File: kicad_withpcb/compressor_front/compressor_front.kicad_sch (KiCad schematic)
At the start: 33 parts, among them J1 MAIN BOARD, SW1 BYPASS, SW2 INT/EXT, SW3 HPF DEFEAT, SW4 LINK, U10 LM3915, U9 LM3914

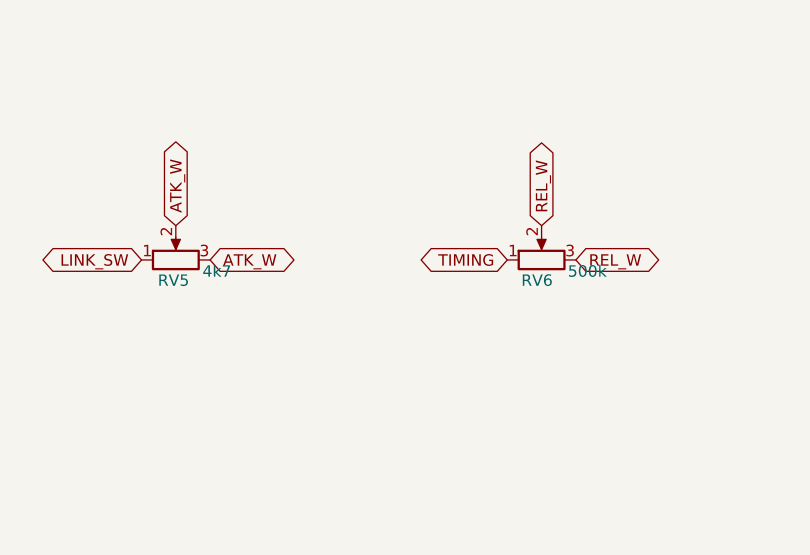
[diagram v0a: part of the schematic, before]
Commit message: Fit real film capacitors on the main board and use Altronics pots for RV5/RV6
RV5 (ATTACK) goes 4k7 -> 10k and RV6 (RELEASE) 500k -> 1M, the nearest
Altronics 9 mm values (R1946, R1950), on the split sheets, both boards
and design.py; the Sim.Params follow (R=10000, R=1e+06).

C5, C8, C9, C10, C14, C15 and C35 were drawn as 7 x 2.5 mm on 5 mm, which
no 2.2-10 uF film part fits. They now use stock KiCad footprints for
in-stock element14 parts:
  10 uF  C5 C8 C15  TDK B32562H1106K000   C_Rect_L16.5mm_W11.8mm_P15.00mm_MKT
  4.7 uF C9 C10     TDK B32562H1475K000   C_Rect_L16.5mm_W7.3mm_P15.00mm_MKT
  2.2 uF C14 C35    KEMET MMK5225K63J06L4 C_Rect_L7.2mm_W7.2mm_P5.00mm_FKS2...

To make room, small parts were re-placed by script (the caps near their
old spots, displaced parts re-homed, then same-footprint parts swapped to
cut wire length; transistors, ICs, connectors and trimmers did not move)
and the main board was re-routed with Freerouting, keeping the original
card-finger stubs. DRC 0 errors, 0 unconnected, schematic parity clean;
ERC 0 errors. The BOM names the element14 parts.
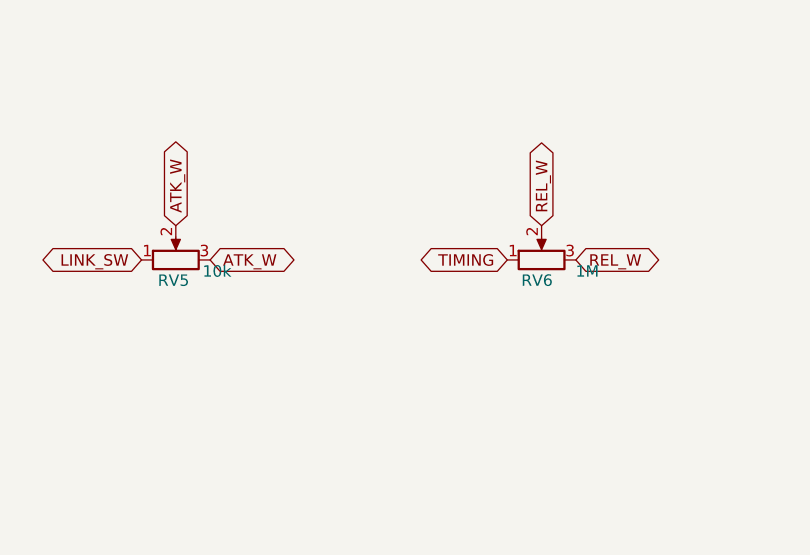
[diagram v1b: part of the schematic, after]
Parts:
- RV5: value 4k7 -> 10k
- RV6: value 500k -> 1M
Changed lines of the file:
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@@
 			)
 		)
-		(property "Value" "500k"
+		(property "Value" "1M"
 			(at 275.59 50.8 90)
 			(show_name no)
@@
 			)
 		)
-		(property "Value" "4k7"
+		(property "Value" "10k"
 			(at 234.442 50.8 90)
 			(show_name no)

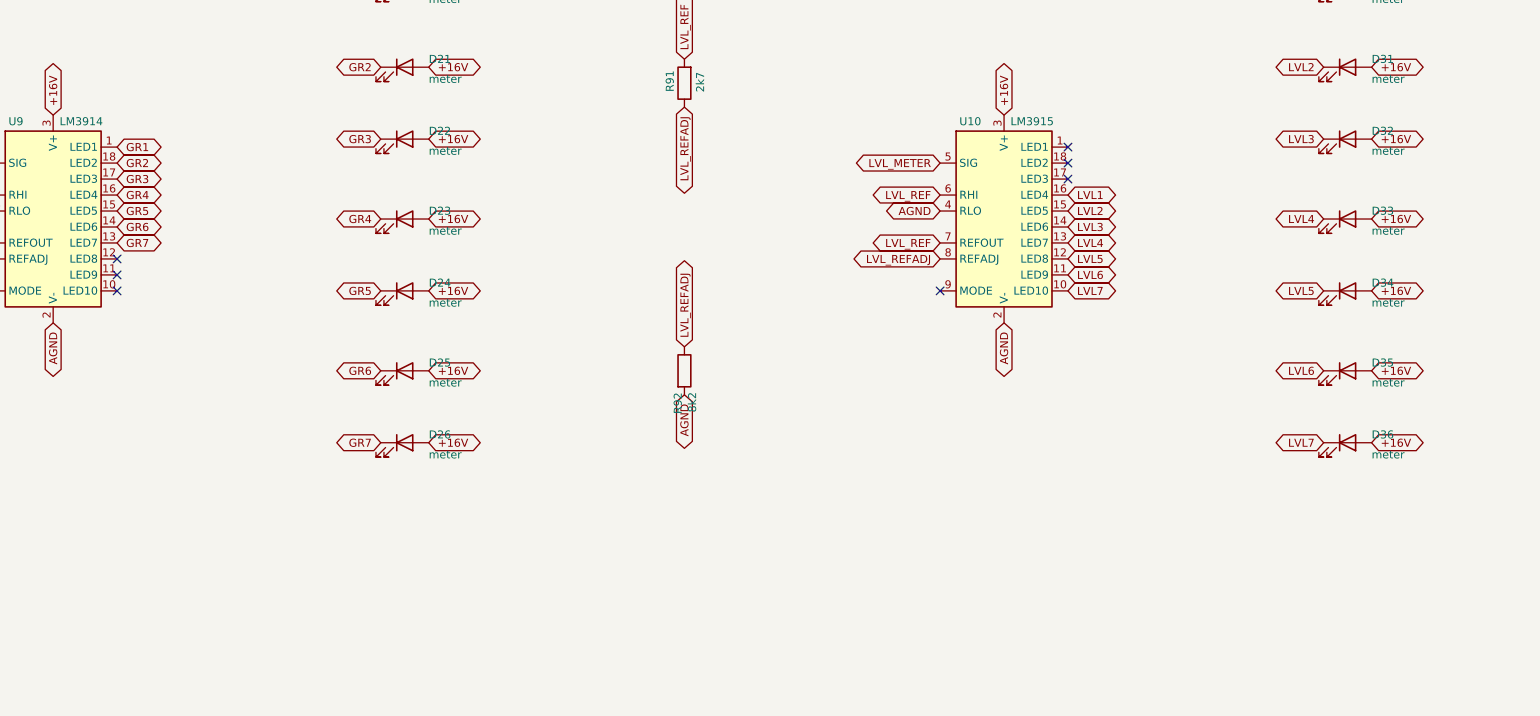
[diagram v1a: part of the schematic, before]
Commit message: Two LM3914 meters with ten LEDs each, simulated (#6)
* Swap the level meter's LM3915 for an LM3914 on outputs 1-7

Nobody stocks the LM3915, so U10 becomes a second LM3914. The LEDs move
to outputs 1-7 and outputs 8-10 join the top LED, giving a 17 dB scale
with no added parts. Front board LVL tracks re-routed; BOM regenerated.

* Give both meters ten LEDs and simulate them

Adds D27-D29 (GR outputs 8-10) and D37-D39 (LVL outputs 8-10) on all three
schematics. The front board's meter columns move to a 3.0 mm pitch with
LVL output 10 at the top; R90/R92 move to a 7.62 mm footprint and C38
turns to clear the LEDs; the affected nets were re-routed. R92 becomes 4k7
so RV8 can set the top LED at +18 dBu. The panel gets the six extra holes.
The LM3914 sim model now has its comparators and LED current sinks, and
tools/sim/meters.py simulates both meters.

* Write up the meter simulation
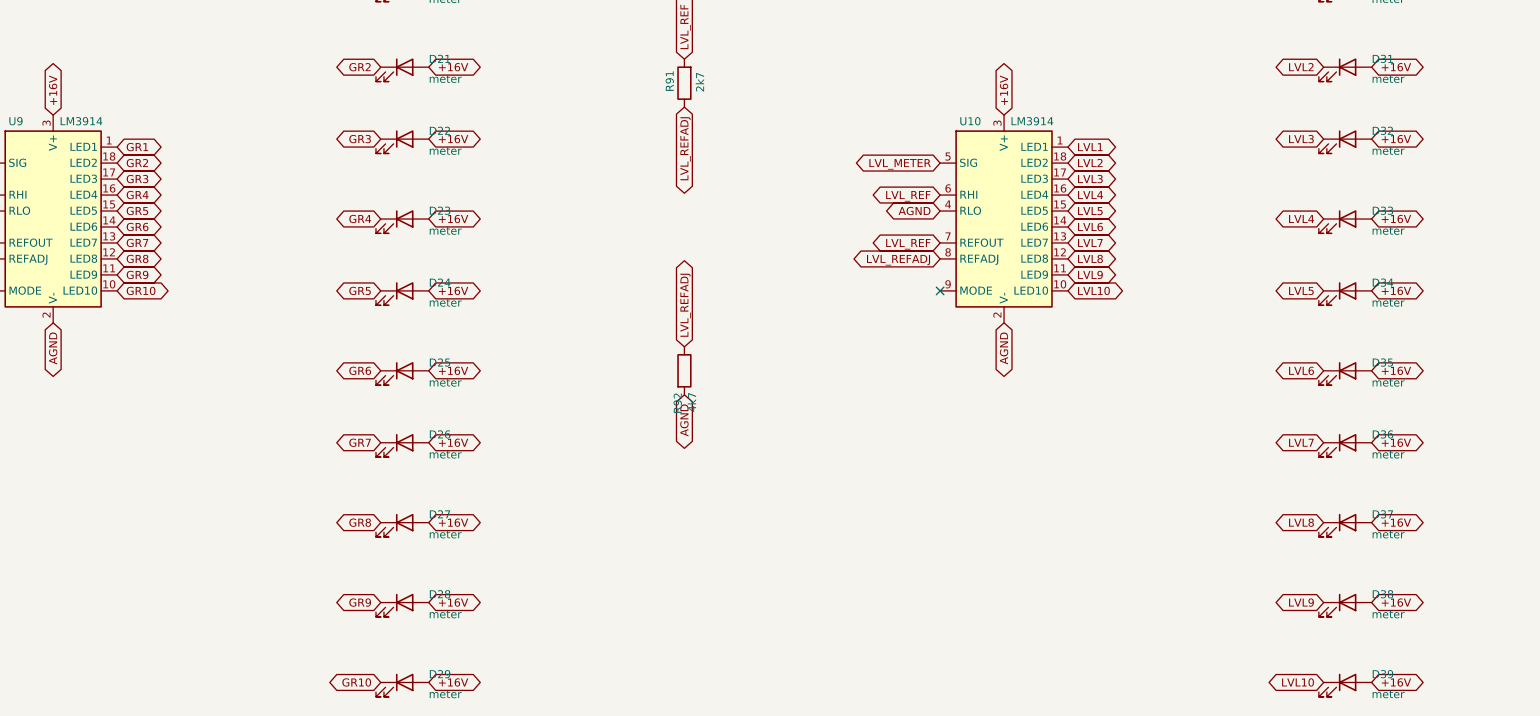
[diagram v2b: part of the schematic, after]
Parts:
- added D27, D28, D29, D37, D38, D39: meter, LED_THT:LED_D2.0mm_W4.0mm_H2.8mm_FlatTop, symbol Device:LED
- R90: footprint Resistor_THT:R_Axial_DIN0207_L6.3mm_D2.5mm_P10.16mm_Horizontal -> Resistor_THT:R_Axial_DIN0207_L6.3mm_D2.5mm_P7.62mm_Horizontal
- R92: value 8k2 -> 4k7; footprint Resistor_THT:R_Axial_DIN0207_L6.3mm_D2.5mm_P10.16mm_Horizontal -> Resistor_THT:R_Axial_DIN0207_L6.3mm_D2.5mm_P7.62mm_Horizontal
- U10: value LM3915 -> LM3914
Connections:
- net +16V: now also D27.2 (A), D28.2 (A), D29.2 (A), D37.2 (A), D38.2 (A), D39.2 (A)
- net LVL1: now also U10.1 (LED1); no longer U10.16 (LED4)
- net LVL2: now also U10.18 (LED2); no longer U10.15 (LED5)
- net LVL3: now also U10.17 (LED3); no longer U10.14 (LED6)
- net LVL4: now also U10.16 (LED4); no longer U10.13 (LED7)
- net LVL5: now also U10.15 (LED5); no longer U10.12 (LED8)
- net LVL6: now also U10.14 (LED6); no longer U10.11 (LED9)
- net LVL7: now also U10.13 (LED7); no longer U10.10 (LED10)
- net GR10: now reaches U9.10 (LED10)
- net GR10: now also D29.1 (K)
- net GR9: now reaches U9.11 (LED9)
- net GR9: now also D28.1 (K)
- net GR8: now reaches U9.12 (LED8)
- net GR8: now also D27.1 (K)
- new net LVL10: D39.1 (K), U10.10 (LED10)
- new net LVL8: D37.1 (K), U10.12 (LED8)
- new net LVL9: D38.1 (K), U10.11 (LED9)
- no-connect marks 8 -> 2

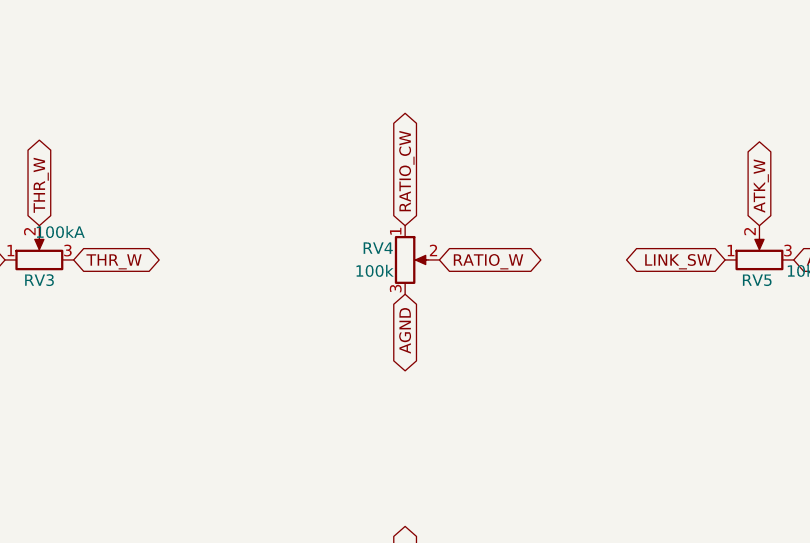
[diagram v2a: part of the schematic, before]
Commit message: Re-route the main board, reverse RATIO, and re-plot the Gerbers for both boards (#7)
* Re-plot the Gerbers for both boards from the current layout

The committed main-board Gerbers were plotted on 2026-10-01, before the film-cap
re-place and re-route, so 119 of their holes no longer match the board. Re-plot
them from the current board, add the front board's set, and zip each for the fab.

tools/plot_fab.sh does both boards in one go so the zips can be refreshed after
every board change. The README gets an Ordering section with the fab settings.

* Re-route the main board: paired IN/OUT, one-piece ground pour

IN+/IN- and OUT+/OUT- run as pairs 0.6 mm apart on the top layer, with
one via each on IN- and OUT- beside the edge fingers. Most other tracks
moved to the top so the bottom AGND pour is one piece (was seven).
DRC 0 errors, 0 unconnected, 0 schematic parity issues. Gerbers re-plotted.

* Swap RATIO's outer pins so clockwise gives a harder ratio

RV4 pin 1 is now AGND and pin 3 RATIO_CW on all three schematics and the
front board (symbol mirrored, front-board tracks re-routed at RV4).
The sim model reads POS={1-RATIO}, so RATIO keeps its meaning and the
results are unchanged. Front-board DRC 0 errors, 0 unconnected, 0 parity;
front Gerbers re-plotted.
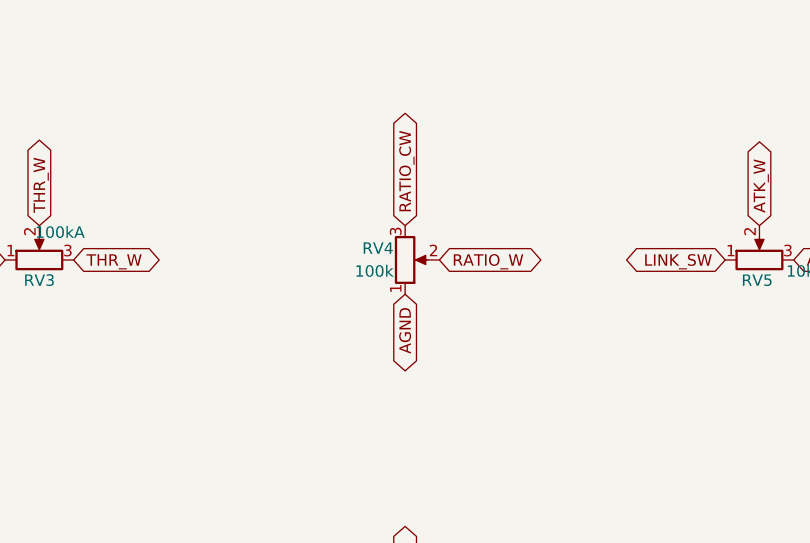
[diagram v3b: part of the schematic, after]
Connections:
- net AGND: now also RV4.1; no longer RV4.3
- net RATIO_CW: now also RV4.3; no longer RV4.1
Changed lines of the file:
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@@
 		(lib_id "Device:R_Potentiometer")
 		(at 190.5 49.53 0)
+		(mirror x)
 		(unit 1)
 		(body_style 1)
